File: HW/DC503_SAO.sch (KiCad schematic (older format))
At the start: 22 parts

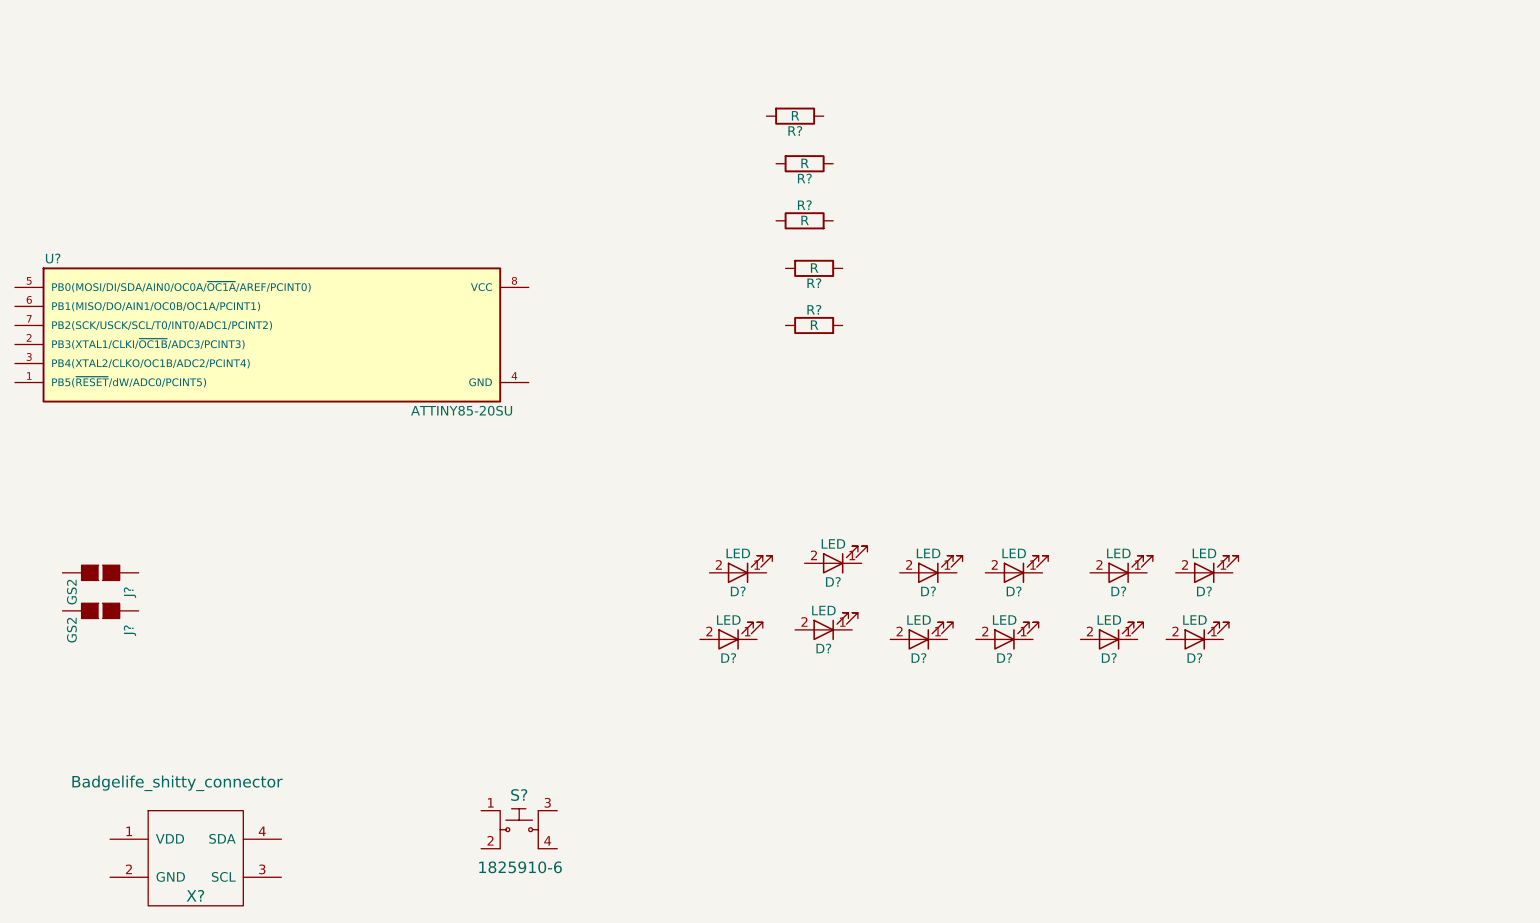
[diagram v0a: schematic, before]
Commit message: wired up SOA connector, switch, and three LEDs
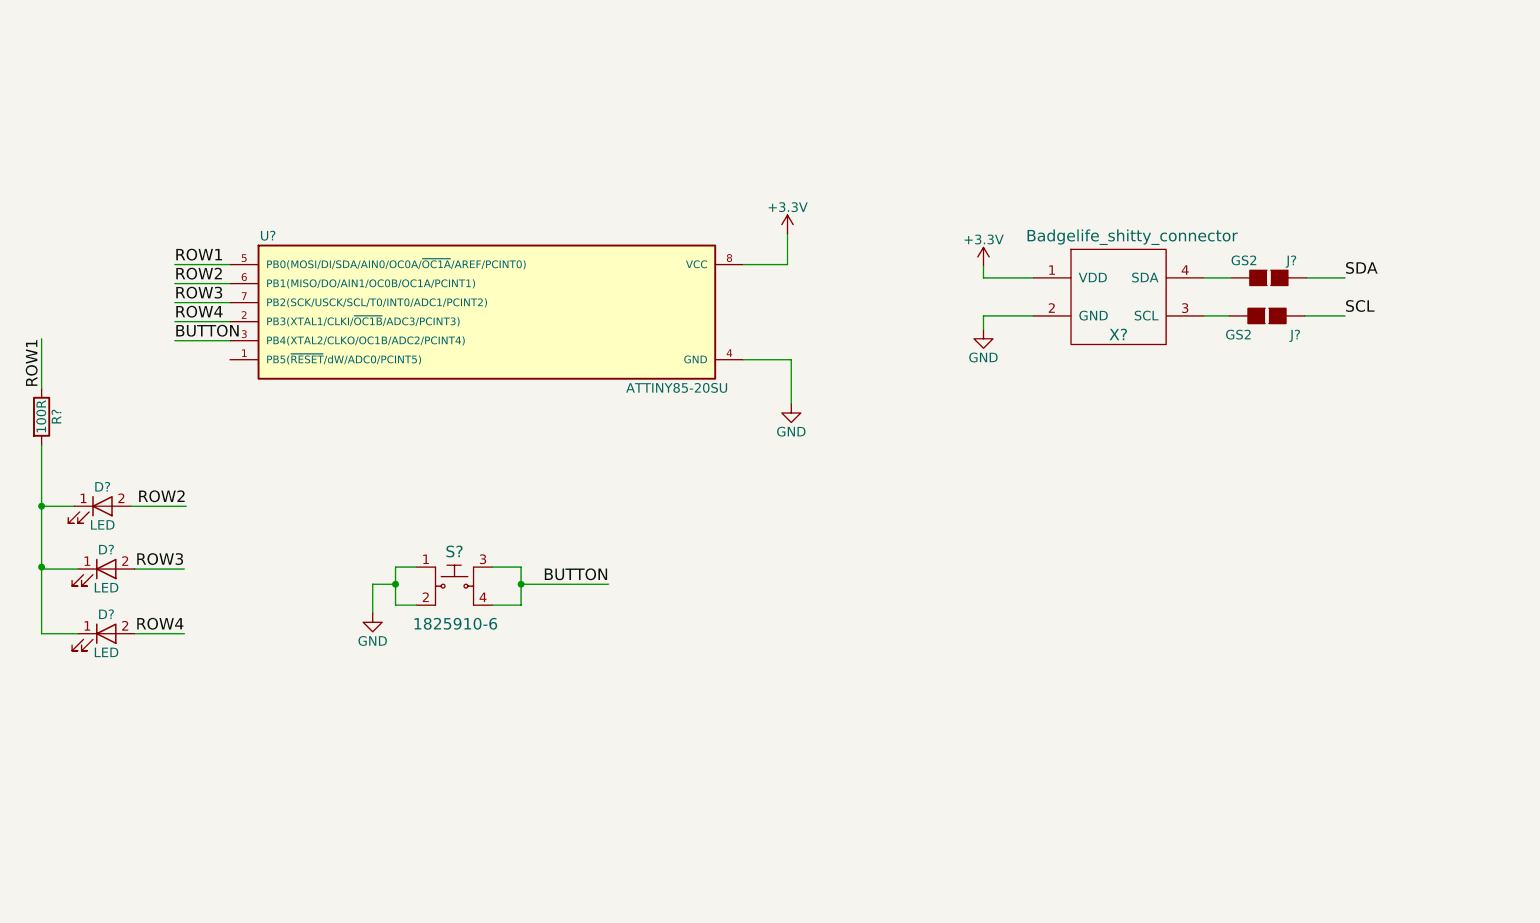
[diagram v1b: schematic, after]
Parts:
- removed D? (x9): LED, symbol LED
- removed R? (x4): R, symbol R
- R?: value R -> 100R
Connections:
- net ROW4: now reaches U?.2 (PB3(XTAL1/CLKI/~OC1B~/ADC3/PCINT3))
- net ROW4: now also D?.2 (A)
- net BUTTON: now reaches U?.3 (PB4(XTAL2/CLKO/OC1B/ADC2/PCINT4))
- net BUTTON: now also S?.3, S?.4
- net GND: now reaches U?.4 (GND)
- net GND: now also S?.1, S?.2, X?.2 (GND)
- net ROW1: now reaches U?.5 (PB0(MOSI/DI/SDA/AIN0/OC0A/~OC1A~/AREF/PCINT0))
- net ROW1: now also R?.1
- net ROW2: now reaches U?.6 (PB1(MISO/DO/AIN1/OC0B/OC1A/PCINT1))
- net ROW2: now also D?.2 (A)
- net ROW3: now reaches U?.7 (PB2(SCK/USCK/SCL/T0/INT0/ADC1/PCINT2))
- net ROW3: now also D?.2 (A)
- net +3V3: now reaches U?.8 (VCC)
- net +3V3: now also X?.1 (VDD)
- net at X?.3 (SCL): now also J?.2 (G2)
- net at X?.4 (SDA): now also J?.2 (G2)
- net at R?.2: now also D?.1 (K), D?.1 (K), D?.1 (K)
- net SCL: now reaches J?.1 (G1)
- net SDA: now reaches J?.1 (G1)
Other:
- moved on the sheet: D?, J?, R?, S?, U?, X?

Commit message: finished LEDs
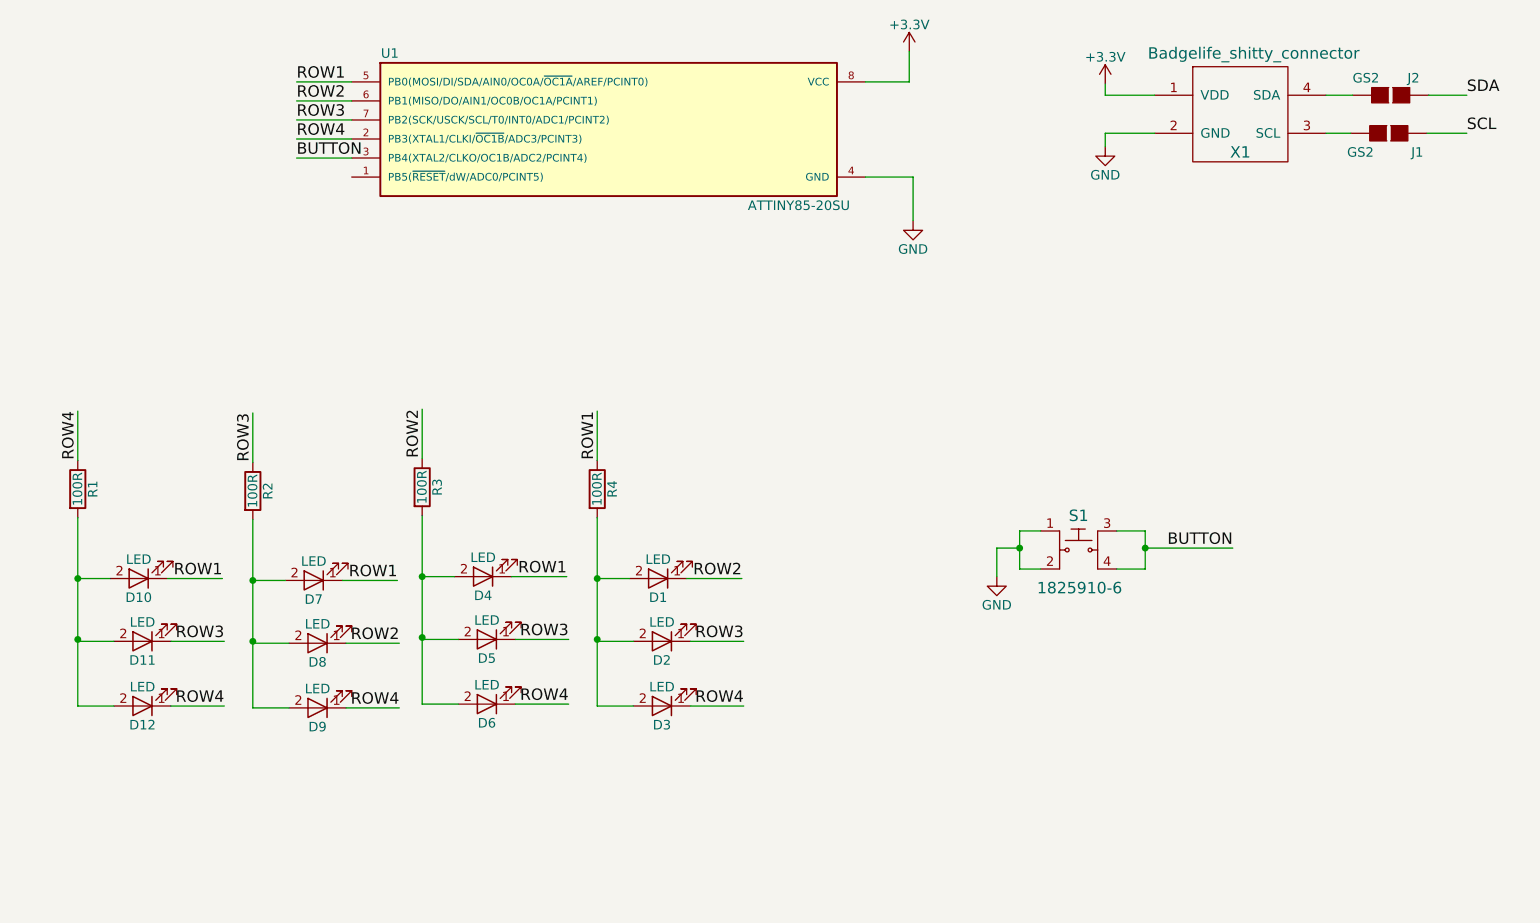
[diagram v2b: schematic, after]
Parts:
- added D10, D11, D12, D4, D5, D6, D7, D8, D9: LED, symbol LED
- added R1, R2, R3: 100R, symbol R
- gave numbers to parts that had none: 9
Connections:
- net ROW1: now also D10.1 (K), D4.1 (K), D7.1 (K)
- net ROW2: now also D1.1 (K), D8.1 (K), R3.1; no longer D1.2 (A)
- net ROW3: now also D2.1 (K), D11.1 (K), D5.1 (K), R2.1; no longer D2.2 (A)
- net ROW4: now also D3.1 (K), D12.1 (K), D6.1 (K), D9.1 (K), R1.1; no longer D3.2 (A)
- new net: D1.2 (A), D2.2 (A), D3.2 (A), R4.2
- new net: D4.2 (A), D5.2 (A), D6.2 (A), R3.2
- new net: D7.2 (A), D8.2 (A), D9.2 (A), R2.2
- new net: D10.2 (A), D11.2 (A), D12.2 (A), R1.2
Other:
- moved on the sheet: D1, D2, D3, J1, J2, R4, S1, U1, X1

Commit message: Fixed footprint issue by adding footprints to PCBnew
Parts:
- D1, D10, D11, D12, D2, D3, D4, D5, D6, D7, D8, D9: footprint (none) -> DC503_SAO:OSRAM_LED
- R1, R2, R3, R4: footprint (none) -> Resistors_SMD:R_0805
- X1: footprint (none) -> SAO:Badgelife-Shitty-2x2

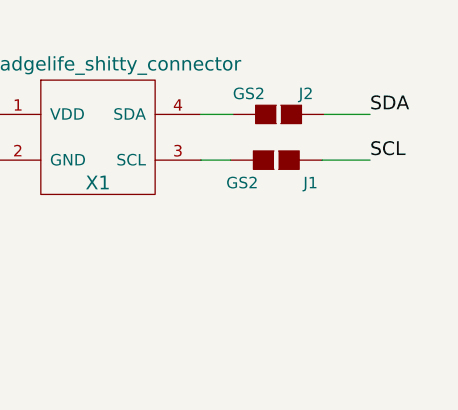
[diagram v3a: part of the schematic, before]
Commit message: moved parts to back layer. Connected I2C pins (not ideally)
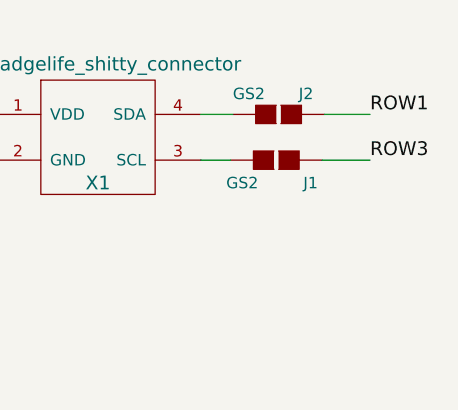
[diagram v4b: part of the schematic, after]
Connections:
- net SCL is gone; now on net ROW3: J1.1 (G1)
- net SDA is gone; now on net ROW1: J2.1 (G1)
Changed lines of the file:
@@
 $EndComp
 Text Label 10630 1590 0    60   ~ 0
-SDA
+ROW1
 Text Label 10630 1790 0    60   ~ 0
-SCL
+ROW3
 Text Label 4480 1520 0    60   ~ 0
 ROW1
